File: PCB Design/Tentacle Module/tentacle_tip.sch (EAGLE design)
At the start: 8 parts, among them U1 ADXL345

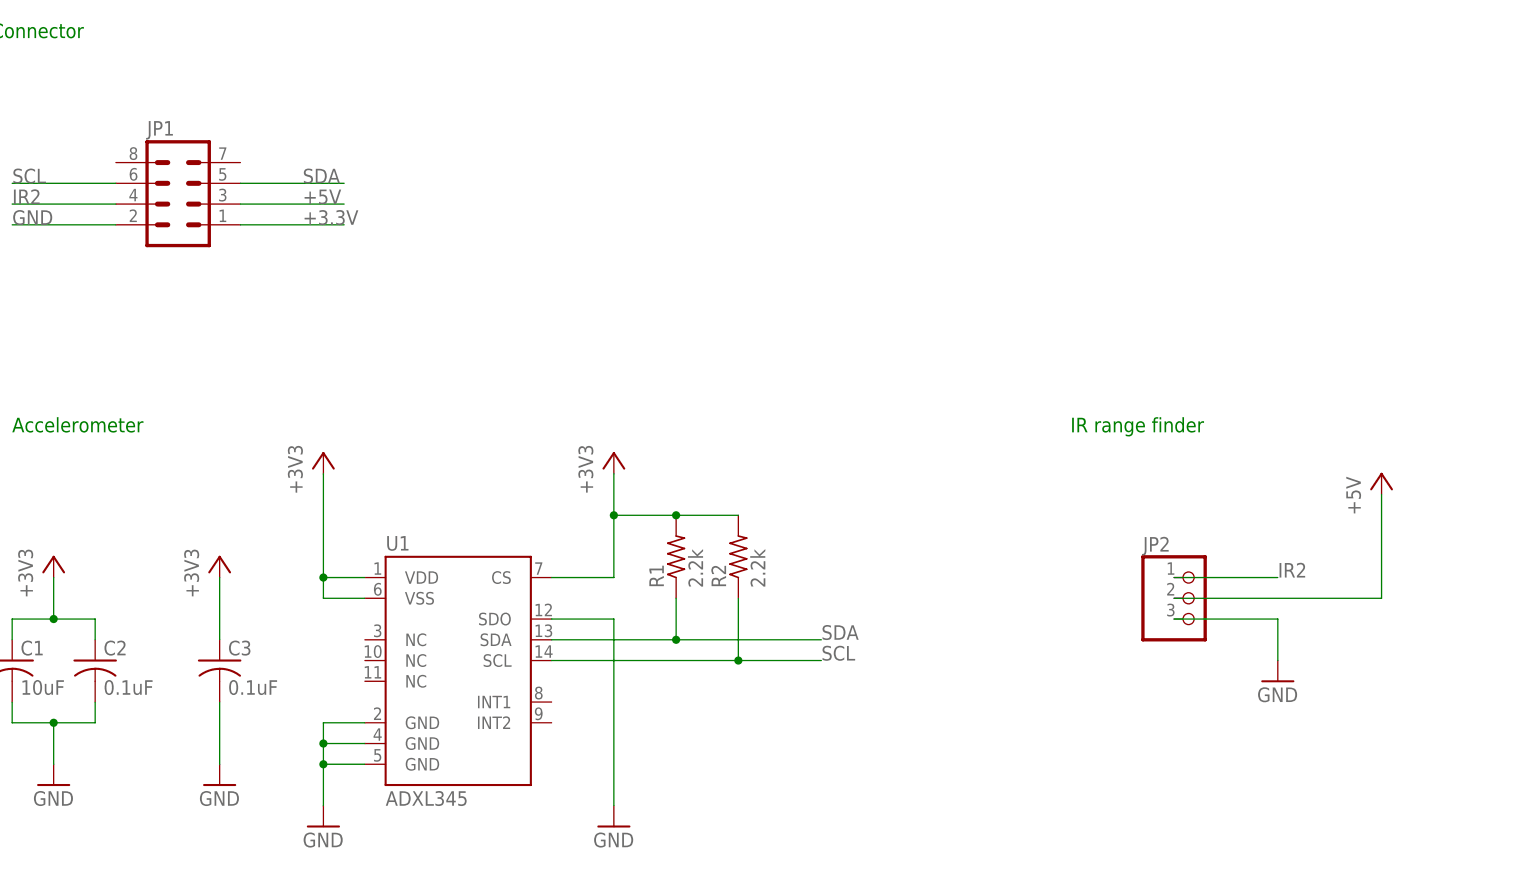
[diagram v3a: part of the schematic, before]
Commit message: fixed the error with order of headers for IR sensor
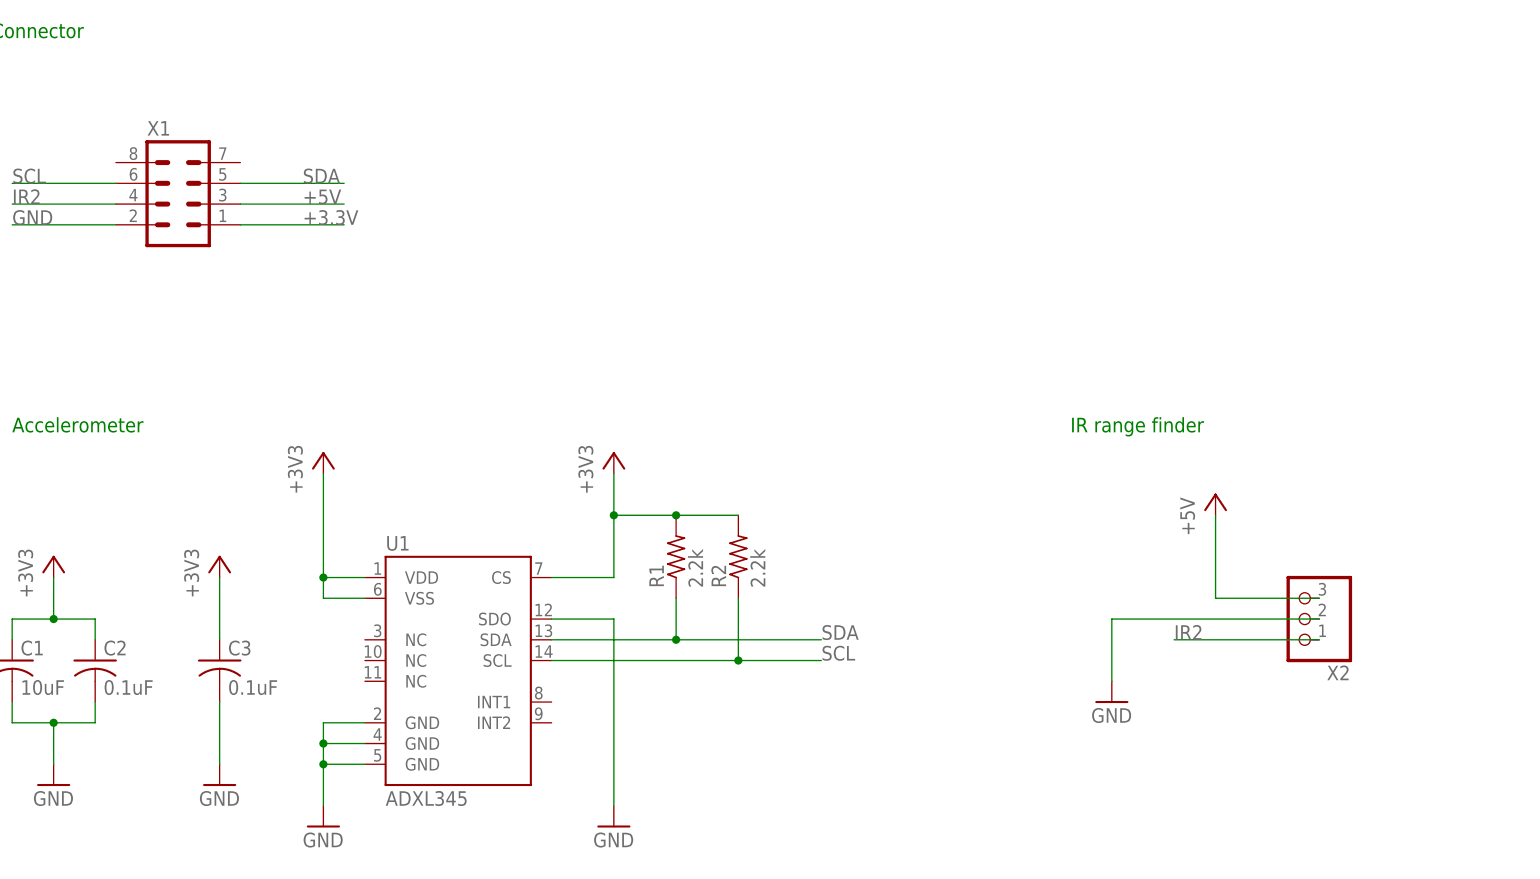
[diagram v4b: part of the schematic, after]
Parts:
- removed JP2: (no value), CBLA_Test_bed_Library:PINHD-1X3/90
- added X2: (no value), CBLA_Test_bed_Library:PINHD-1X3/90
- renumbered JP1 to X1
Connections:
- net +5V: now also X2.3; no longer JP2.2
- net GND: now also X2.2; no longer JP2.3
- net IR2: now also X2.1; no longer JP2.1
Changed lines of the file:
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@@
 </classes>
 <parts>
+<part name="GND3" library="supply1" deviceset="GND" device=""/>
+<part name="C2" library="rcl" deviceset="C-US" device="C0603" value="0.1uF"/>
 <part name="GND1" library="supply1" deviceset="GND" device=""/>
-<part name="C2" library="rcl" deviceset="C-US" device="C0603" value="0.1uF"/>
-<part name="GND3" library="supply1" deviceset="GND" device=""/>
 <part name="C3" library="rcl" deviceset="C-US" device="C0603" value="0.1uF"/>
-<part name="GND4" library="supply1" deviceset="GND" device=""/>
+<part name="GND2" library="supply1" deviceset="GND" device=""/>
 <part name="C1" library="rcl" deviceset="C-US" device="C1206" value="10uF"/>
 <part name="U1" library="CBLA_Test_bed_Library" deviceset="ADXL345" device="LONG" value="ADXL345"/>
-<part name="+3V1" library="supply1" deviceset="+3V3" device=""/>
-<part name="+5V" library="supply1" deviceset="+5V" device=""/>
-<part name="+3V2" library="supply1" deviceset="+3V3" device=""/>
-<part name="+3V3" library="supply1" deviceset="+3V3" device=""/>
-<part name="+3V4" library="supply1" deviceset="+3V3" device=""/>
-<part name="GND2" library="supply1" deviceset="GND" device=""/>
+<part name="+3V33" library="supply1" deviceset="+3V3" device=""/>
+<part name="P+1" library="supply1" deviceset="+5V" device=""/>
+<part name="+3V32" library="supply1" deviceset="+3V3" device=""/>
+<part name="+3V31" library="supply1" deviceset="+3V3" device=""/>
+<part name="+3V34" library="supply1" deviceset="+3V3" device=""/>
+<part name="GND4" library="supply1" deviceset="GND" device=""/>
 <part name="R1" library="rcl" deviceset="R-US_" device="R0603" value="2.2k"/>
 <part name="R2" library="rcl" deviceset="R-US_" device="R0603" value="2.2k"/>
-<part name="JP2" library="CBLA_Test_bed_Library" deviceset="PINHD-1X3" device="/90"/>
+<part name="X2" library="CBLA_Test_bed_Library" deviceset="PINHD-1X3" device="/90"/>
 <part name="GND5" library="supply1" deviceset="GND" device=""/>
-<part name="JP1" library="CBLA_Test_bed_Library" deviceset="MA04-2" device=""/>
+<part name="X1" library="CBLA_Test_bed_Library" deviceset="MA04-2" device=""/>
 </parts>
 <sheets>
@@
 </plain>
 <instances>
-<instance part="GND1" gate="1" x="68.58" y="68.58"/>
+<instance part="GND3" gate="1" x="68.58" y="68.58"/>
 <instance part="C2" gate="G$1" x="40.64" y="88.9"/>
-<instance part="GND3" gate="1" x="35.56" y="73.66"/>
+<instance part="GND1" gate="1" x="35.56" y="73.66"/>
 <instance part="C3" gate="G$1" x="55.88" y="88.9"/>
-<instance part="GND4" gate="1" x="55.88" y="73.66"/>
+<instance part="GND2" gate="1" x="55.88" y="73.66"/>
 <instance part="C1" gate="G$1" x="30.48" y="88.9"/>
 <instance part="U1" gate="G$1" x="83.82" y="88.9"/>
-<instance part="+3V1" gate="G$1" x="68.58" y="114.3"/>
-<instance part="+5V" gate="1" x="198.12" y="111.76"/>
-<instance part="+3V2" gate="G$1" x="55.88" y="101.6"/>
-<instance part="+3V3" gate="G$1" x="35.56" y="101.6"/>
-<instance part="+3V4" gate="G$1" x="104.14" y="114.3"/>
-<instance part="GND2" gate="1" x="104.14" y="68.58"/>
+<instance part="+3V33" gate="G$1" x="68.58" y="114.3"/>
+<instance part="P+1" gate="1" x="177.8" y="109.22"/>
+<instance part="+3V32" gate="G$1" x="55.88" y="101.6"/>
+<instance part="+3V31" gate="G$1" x="35.56" y="101.6"/>
+<instance part="+3V34" gate="G$1" x="104.14" y="114.3"/>
+<instance part="GND4" gate="1" x="104.14" y="68.58"/>
 <instance part="R1" gate="G$1" x="111.76" y="101.6" rot="R90"/>
 <instance part="R2" gate="G$1" x="119.38" y="101.6" rot="R90"/>
-<instance part="JP2" gate="A" x="175.26" y="96.52"/>
-<instance part="GND5" gate="1" x="185.42" y="86.36"/>
-<instance part="JP1" gate="G$1" x="50.8" y="147.32"/>
+<instance part="X2" gate="A" x="187.96" y="93.98" rot="R180"/>
+<instance part="GND5" gate="1" x="165.1" y="83.82"/>
+<instance part="X1" gate="G$1" x="50.8" y="147.32"/>
 </instances>
 <busses>
@@
 <net name="IR2" class="0">
 <segment>
-<pinref part="JP2" gate="A" pin="1"/>
-<wire x1="172.72" y1="99.06" x2="185.42" y2="99.06" width="0.1524" layer="91"/>
-<label x="185.42" y="99.06" size="1.778" layer="95"/>
-</segment>
-<segment>
-<pinref part="JP1" gate="G$1" pin="4"/>
+<pinref part="X2" gate="A" pin="1"/>
+<wire x1="190.5" y1="91.44" x2="172.72" y2="91.44" width="0.1524" layer="91"/>
+<label x="172.72" y="91.44" size="1.778" layer="95"/>
+</segment>
+<segment>
+<pinref part="X1" gate="G$1" pin="4"/>
 <wire x1="43.18" y1="144.78" x2="30.48" y2="144.78" width="0.1524" layer="91"/>
 <label x="30.48" y="144.78" size="1.778" layer="95"/>
@@
 <net name="+5V" class="0">
 <segment>
-<pinref part="JP2" gate="A" pin="2"/>
-<pinref part="+5V" gate="1" pin="+5V"/>
-<wire x1="172.72" y1="96.52" x2="198.12" y2="96.52" width="0.1524" layer="91"/>
-<wire x1="198.12" y1="96.52" x2="198.12" y2="109.22" width="0.1524" layer="91"/>
-</segment>
-<segment>
-<pinref part="JP1" gate="G$1" pin="3"/>
+<pinref part="P+1" gate="1" pin="+5V"/>
+<wire x1="177.8" y1="96.52" x2="177.8" y2="106.68" width="0.1524" layer="91"/>
+<pinref part="X2" gate="A" pin="3"/>
+<wire x1="190.5" y1="96.52" x2="177.8" y2="96.52" width="0.1524" layer="91"/>
+</segment>
+<segment>
+<pinref part="X1" gate="G$1" pin="3"/>
 <wire x1="58.42" y1="144.78" x2="71.12" y2="144.78" width="0.1524" layer="91"/>
 <label x="66.04" y="144.78" size="1.778" layer="95"/>
@@
 <pinref part="C1" gate="G$1" pin="1"/>
 <pinref part="C2" gate="G$1" pin="1"/>
-<pinref part="+3V3" gate="G$1" pin="+3V3"/>
+<pinref part="+3V31" gate="G$1" pin="+3V3"/>
 </segment>
 <segment>
@@
 <pinref part="U1" gate="G$1" pin="VDD"/>
 <pinref part="U1" gate="G$1" pin="VSS"/>
-<pinref part="+3V1" gate="G$1" pin="+3V3"/>
+<pinref part="+3V33" gate="G$1" pin="+3V3"/>
 </segment>
 <segment>
 <wire x1="55.88" y1="91.44" x2="55.88" y2="99.06" width="0.1524" layer="91"/>
 <pinref part="C3" gate="G$1" pin="1"/>
-<pinref part="+3V2" gate="G$1" pin="+3V3"/>
-</segment>
-<segment>
-<pinref part="JP1" gate="G$1" pin="1"/>
+<pinref part="+3V32" gate="G$1" pin="+3V3"/>
+</segment>
+<segment>
+<pinref part="X1" gate="G$1" pin="1"/>
 <wire x1="58.42" y1="142.24" x2="71.12" y2="142.24" width="0.1524" layer="91"/>
 <label x="66.04" y="142.24" size="1.778" layer="95"/>
 </segment>
 <segment>
-<pinref part="+3V4" gate="G$1" pin="+3V3"/>
+<pinref part="+3V34" gate="G$1" pin="+3V3"/>
 <wire x1="104.14" y1="111.76" x2="104.14" y2="106.68" width="0.1524" layer="91"/>
 <pinref part="U1" gate="G$1" pin="CS"/>
@@
 <junction x="68.58" y="78.74"/>
 <junction x="68.58" y="76.2"/>
-<pinref part="GND1" gate="1" pin="GND"/>
+<pinref part="GND3" gate="1" pin="GND"/>
 <pinref part="U1" gate="G$1" pin="GND@4"/>
 <pinref part="U1" gate="G$1" pin="GND@5"/>
@@
 <wire x1="55.88" y1="76.2" x2="55.88" y2="83.82" width="0.1524" layer="91"/>
 <pinref part="C3" gate="G$1" pin="2"/>
-<pinref part="GND4" gate="1" pin="GND"/>
+<pinref part="GND2" gate="1" pin="GND"/>
 </segment>
 <segment>
@@
 <wire x1="35.56" y1="81.28" x2="35.56" y2="76.2" width="0.1524" layer="91"/>
 <pinref part="C1" gate="G$1" pin="2"/>
-<pinref part="GND3" gate="1" pin="GND"/>
+<pinref part="GND1" gate="1" pin="GND"/>
 <pinref part="C2" gate="G$1" pin="2"/>
 <wire x1="35.56" y1="81.28" x2="40.64" y2="81.28" width="0.1524" layer="91"/>
@@
 <segment>
 <pinref part="U1" gate="G$1" pin="SDO"/>
-<pinref part="GND2" gate="1" pin="GND"/>
+<pinref part="GND4" gate="1" pin="GND"/>
 <wire x1="96.52" y1="93.98" x2="104.14" y2="93.98" width="0.1524" layer="91"/>
 <wire x1="104.14" y1="93.98" x2="104.14" y2="71.12" width="0.1524" layer="91"/>
 </segment>
 <segment>
-<pinref part="JP2" gate="A" pin="3"/>
-<wire x1="172.72" y1="93.98" x2="185.42" y2="93.98" width="0.1524" layer="91"/>
 <pinref part="GND5" gate="1" pin="GND"/>
-<wire x1="185.42" y1="93.98" x2="185.42" y2="88.9" width="0.1524" layer="91"/>
-</segment>
-<segment>
-<pinref part="JP1" gate="G$1" pin="2"/>
+<wire x1="165.1" y1="93.98" x2="165.1" y2="86.36" width="0.1524" layer="91"/>
+<pinref part="X2" gate="A" pin="2"/>
+<wire x1="190.5" y1="93.98" x2="165.1" y2="93.98" width="0.1524" layer="91"/>
+</segment>
+<segment>
+<pinref part="X1" gate="G$1" pin="2"/>
 <wire x1="43.18" y1="142.24" x2="30.48" y2="142.24" width="0.1524" layer="91"/>
 <label x="30.48" y="142.24" size="1.778" layer="95"/>
@@
 <net name="SCL" class="0">
 <segment>
-<pinref part="JP1" gate="G$1" pin="6"/>
+<pinref part="X1" gate="G$1" pin="6"/>
 <wire x1="43.18" y1="147.32" x2="30.48" y2="147.32" width="0.1524" layer="91"/>
 <label x="30.48" y="147.32" size="1.778" layer="95"/>
@@
 <net name="SDA" class="0">
 <segment>
-<pinref part="JP1" gate="G$1" pin="5"/>
+<pinref part="X1" gate="G$1" pin="5"/>
 <wire x1="58.42" y1="147.32" x2="71.12" y2="147.32" width="0.1524" layer="91"/>
 <label x="66.04" y="147.32" size="1.778" layer="95"/>

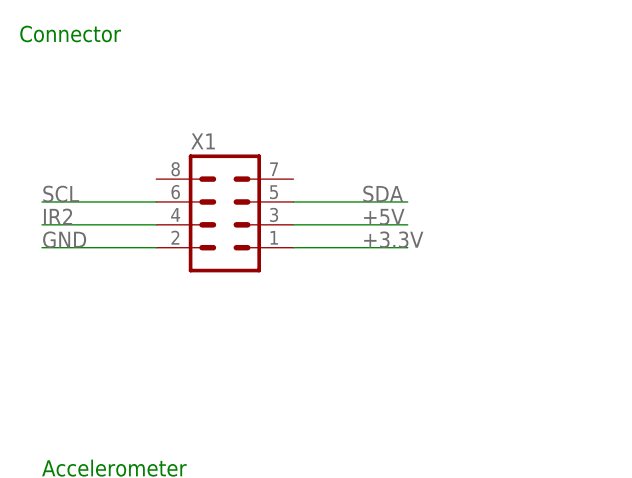
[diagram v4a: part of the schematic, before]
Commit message: Swapped the SDA and SCL pins on the Tentacle tip connector
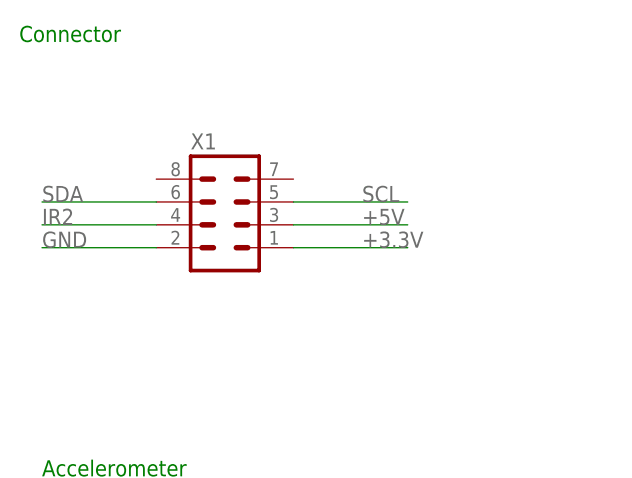
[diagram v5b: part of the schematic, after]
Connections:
- net SCL: now also X1.5; no longer X1.6
- net SDA: now also X1.6; no longer X1.5
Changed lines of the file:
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@@
 <net name="SCL" class="0">
-<segment>
-<pinref part="X1" gate="G$1" pin="6"/>
-<wire x1="43.18" y1="147.32" x2="30.48" y2="147.32" width="0.1524" layer="91"/>
-<label x="30.48" y="147.32" size="1.778" layer="95"/>
-</segment>
 <segment>
 <pinref part="U1" gate="G$1" pin="SCL"/>
@@
 <label x="129.54" y="88.9" size="1.778" layer="95"/>
 </segment>
-</net>
-<net name="SDA" class="0">
 <segment>
 <pinref part="X1" gate="G$1" pin="5"/>
@@
 <label x="66.04" y="147.32" size="1.778" layer="95"/>
 </segment>
+</net>
+<net name="SDA" class="0">
 <segment>
 <pinref part="R1" gate="G$1" pin="1"/>
@@
 <pinref part="U1" gate="G$1" pin="SDA"/>
 </segment>
+<segment>
+<pinref part="X1" gate="G$1" pin="6"/>
+<wire x1="43.18" y1="147.32" x2="30.48" y2="147.32" width="0.1524" layer="91"/>
+<label x="30.48" y="147.32" size="1.778" layer="95"/>
+</segment>
 </net>
